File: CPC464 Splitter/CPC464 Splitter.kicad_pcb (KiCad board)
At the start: 2 copper layers, 81.9 x 40.6 mm, 21 parts, among them J1 Joystick 0, J2 Joystick 1, J3 CPC IDC, M1 Mounting, M2 Mounting, M3 Mounting, M4 Mounting, M5 Mounting, M6 Mounting

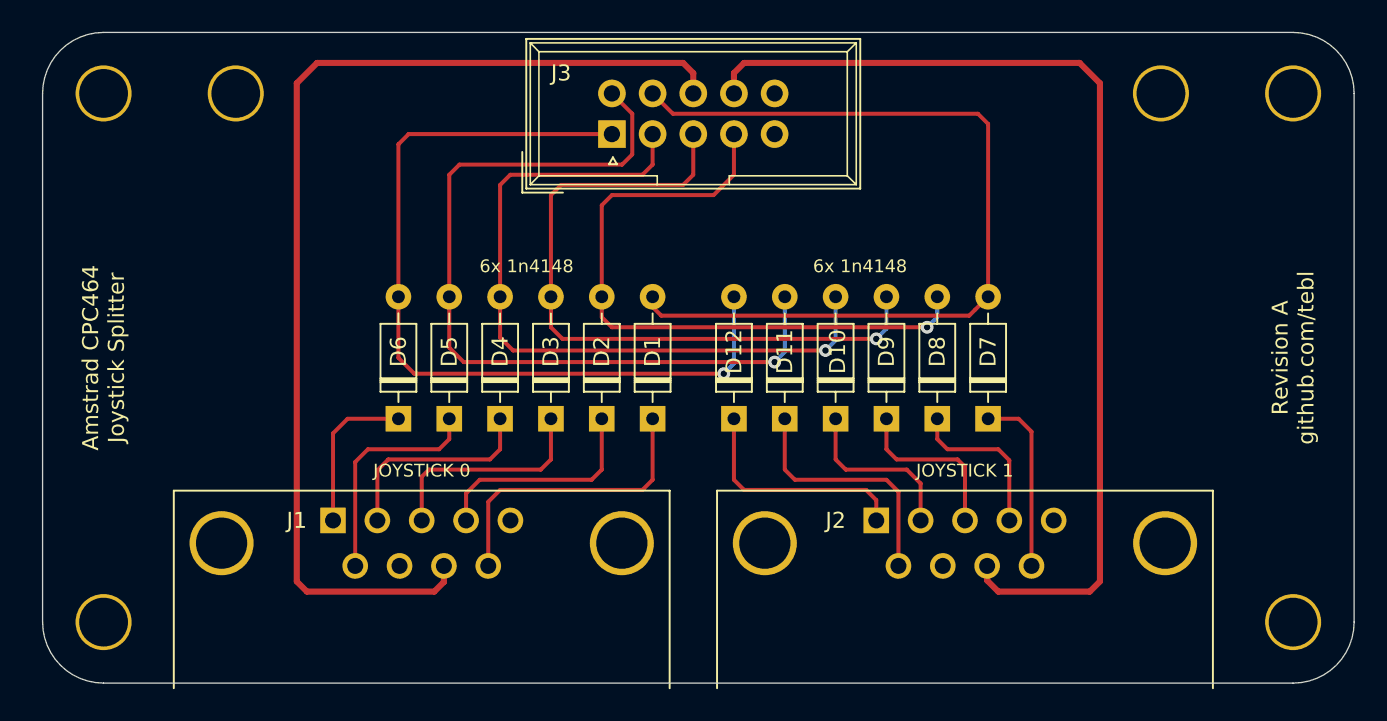
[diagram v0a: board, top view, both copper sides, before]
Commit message: Added reversible faceplate
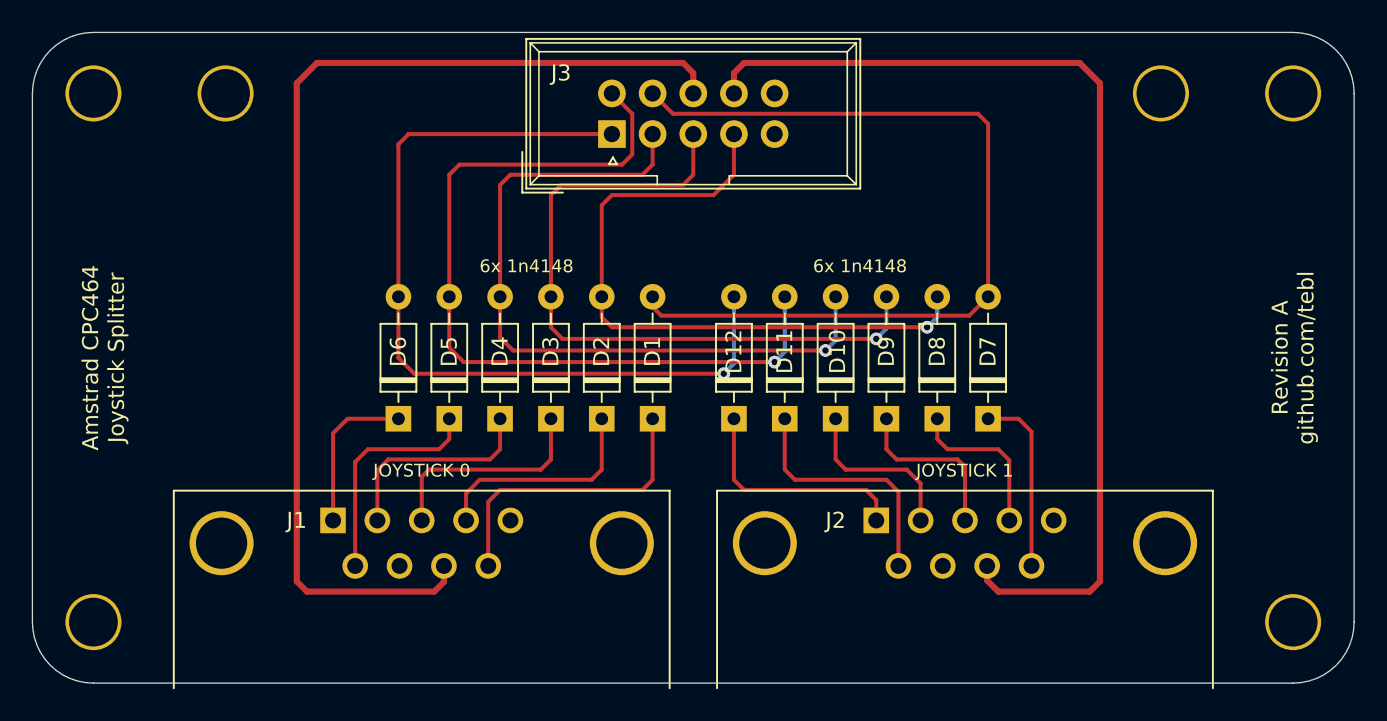
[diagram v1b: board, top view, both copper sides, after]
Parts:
- moved M1 0.64 mm to (102.2, 108.6)
- moved M3 0.64 mm to (102.2, 75.6)
- moved M6 0.64 mm to (110.5, 75.6)
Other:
- board size 81.9 x 40.6 mm -> 82.5 x 40.6 mm
